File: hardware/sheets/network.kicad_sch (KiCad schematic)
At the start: 36 parts, among them J1 RJ45_LED, T1 13F-39MNL, U1 RTL8019AS, U2 AT93C46, U3 74LVC125A, U4 74LVC245A, U5 74HC138, Y1 20MHz

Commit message: addr_decode: hardwire LPT/IDE bases; centralize NIC + video disables (JP1-JP6)
LPT fixed at 0x378, IDE at 0x300 -- both base straps and their pull-ups
deleted ('138 ~Y1 now NC, the '00's ~A5 gate spare, IDE OR-leg takes raw
A5). The NIC and video disable jumpers move to addr_decode as JP5/JP6
with the same fit-to-disable sense as the rest: their gating hardware
stays local (the NIC's isolation '125 inside the 5V island, video's
firmware boot strap on GPIO42), only the jumper levels cross as
mxbus.PRIV_DIS -- video's documented firmware polarity inverts (high =
disabled; no firmware exists yet). Disable row is now a uniform JP1-JP6
(COM1/COM2/LPT/IDE/NIC/VID), bare board runs everything; network JP1/R6
and video JP1/R30 deleted, VID_BASE becomes video JP1. card_video's
wrapper re-adds a local DIS_VID strap (the documented PRIV lift
pattern). Docs/tables/decision logs aligned.

Co-Authored-By: Claude Fable 5 <noreply@anthropic.com>
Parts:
- removed JP1: NET_EN, Connector_PinHeader_2.54mm:PinHeader_1x02_P2.54mm_Vertical, symbol Connector_Generic:Conn_01x02
- removed R6: 10k, Resistor_SMD:R_0603_1608Metric, symbol Device:R
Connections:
- net ~{NET_EN} renamed DIS_NIC
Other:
- note added: "Disable = addr_decode JP5 (DIS_NIC high) -> '125 tri-states IRQ2 AND forces chip AEN high (all I/O ignored). Fully releases the bus for a sidecar card. Enabled by default (no jumper)."
- note removed: "JP1 closed = NIC enabled; open = R6 parks ~{NET_EN} high -> '125 tri-states IRQ2 AND forces chip AEN high (all I/O ignored). Fully releases the bus for a sidecar card."

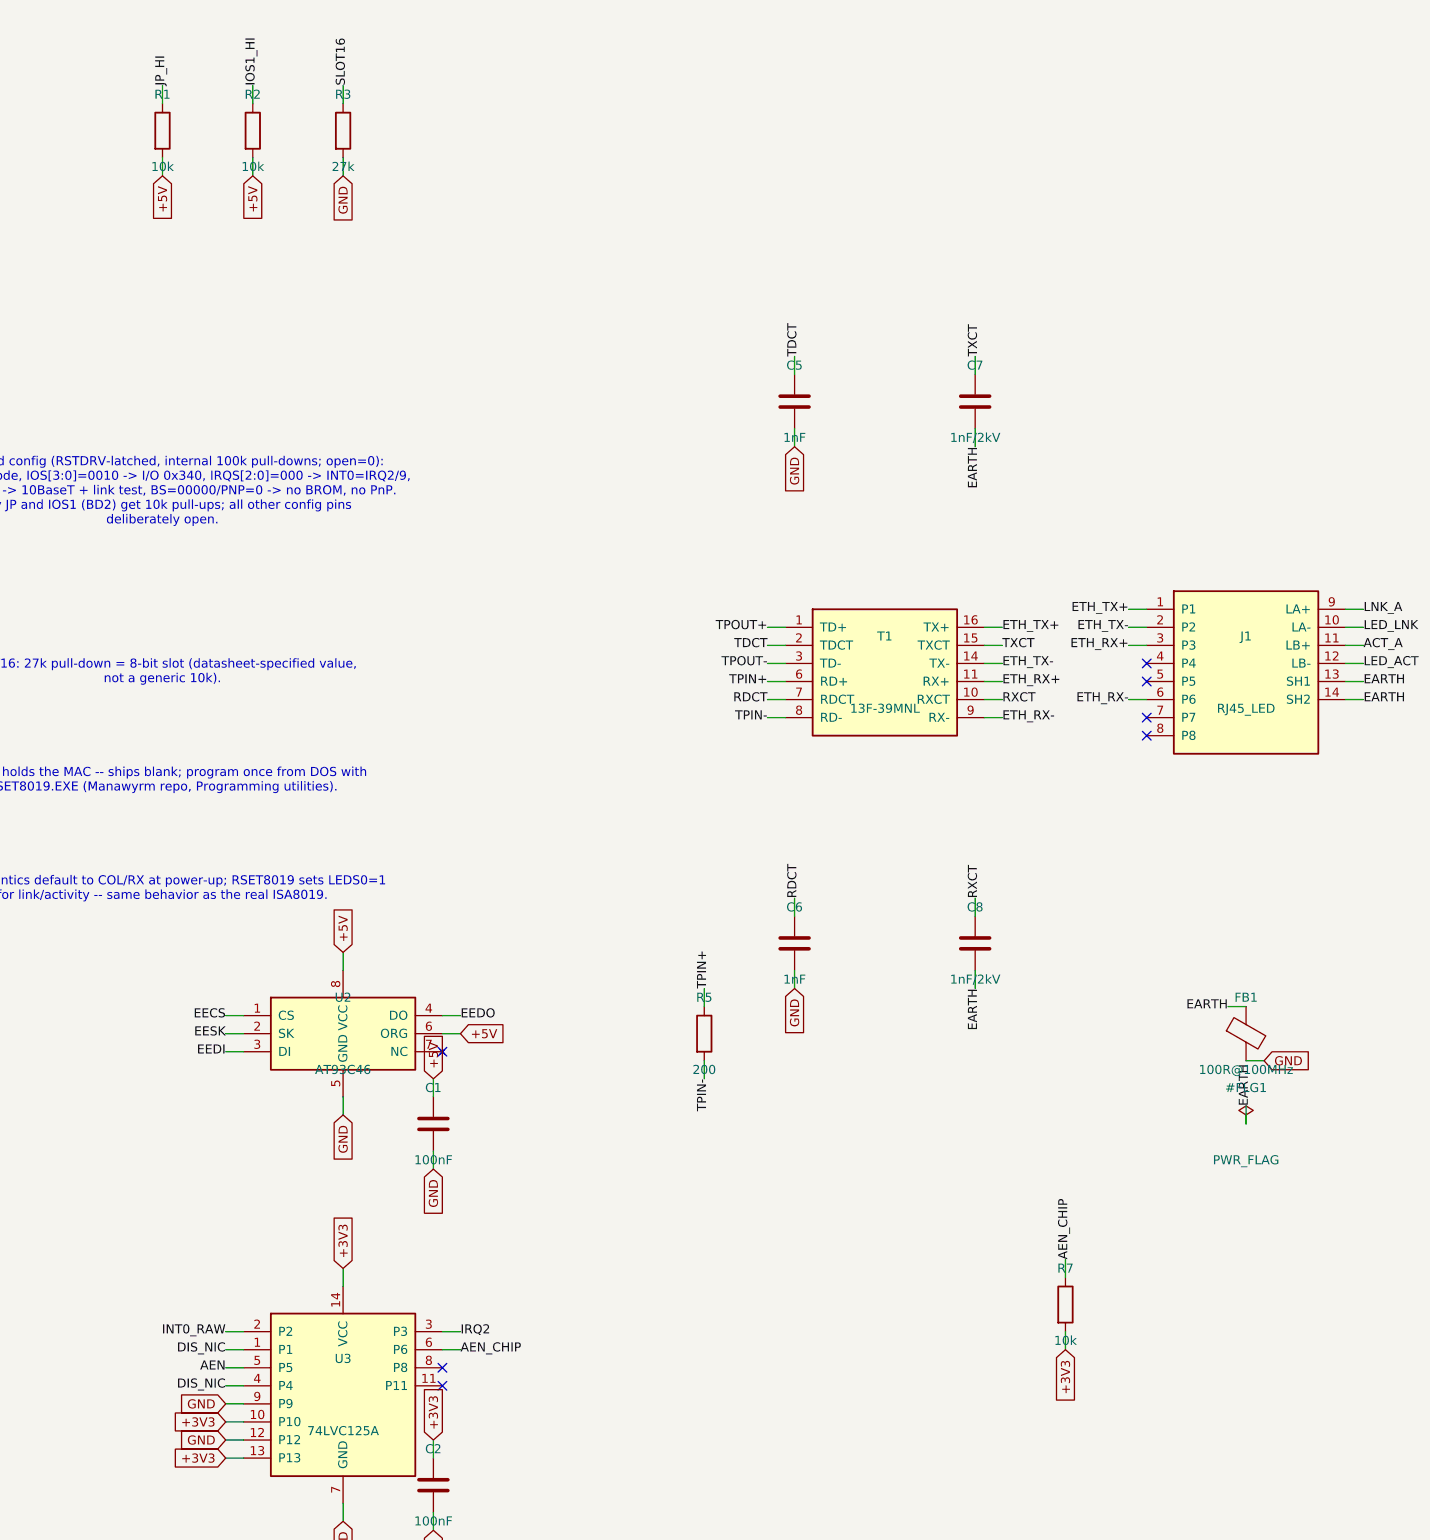
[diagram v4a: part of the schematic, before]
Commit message: Passives: basic-library audit + 4x resistor-array pull consolidation
Audit: every discrete R/C value was already JLC basic except the ferrite
beads -- swapped to basic Murata BLM18PG121SN1D (C14709, 120R@100MHz,
same family/role). The 100uF electrolytic and buck inductor stay
extended (zero fee-free parts exist in those subcategories). Pruned the
orphaned 5V-era 47nF/330nF MAX3241 cap entries.

Pull consolidation: 65 discrete 10k/4.7k rail pulls across 8 sheets
collapse into 18 basic 4-element isolated arrays (4D03WGJ0103T5E /
4D03WGJ0472T5E, element k = pins k/9-k; new mxbus.r_pack4 helper).
Isolated elements let packs mix rails; every net keeps its exact rail
and semantics (verified element-by-element in the netlist). RC/divider/
series/I2C resistors stay discrete. Board 452 -> 406 components; also
de-risks the sole basic 10k 0603 line (0 stock at audit). Audit
recorded in jlcpcb-sourcing.md.

Co-Authored-By: Claude Fable 5 <noreply@anthropic.com>
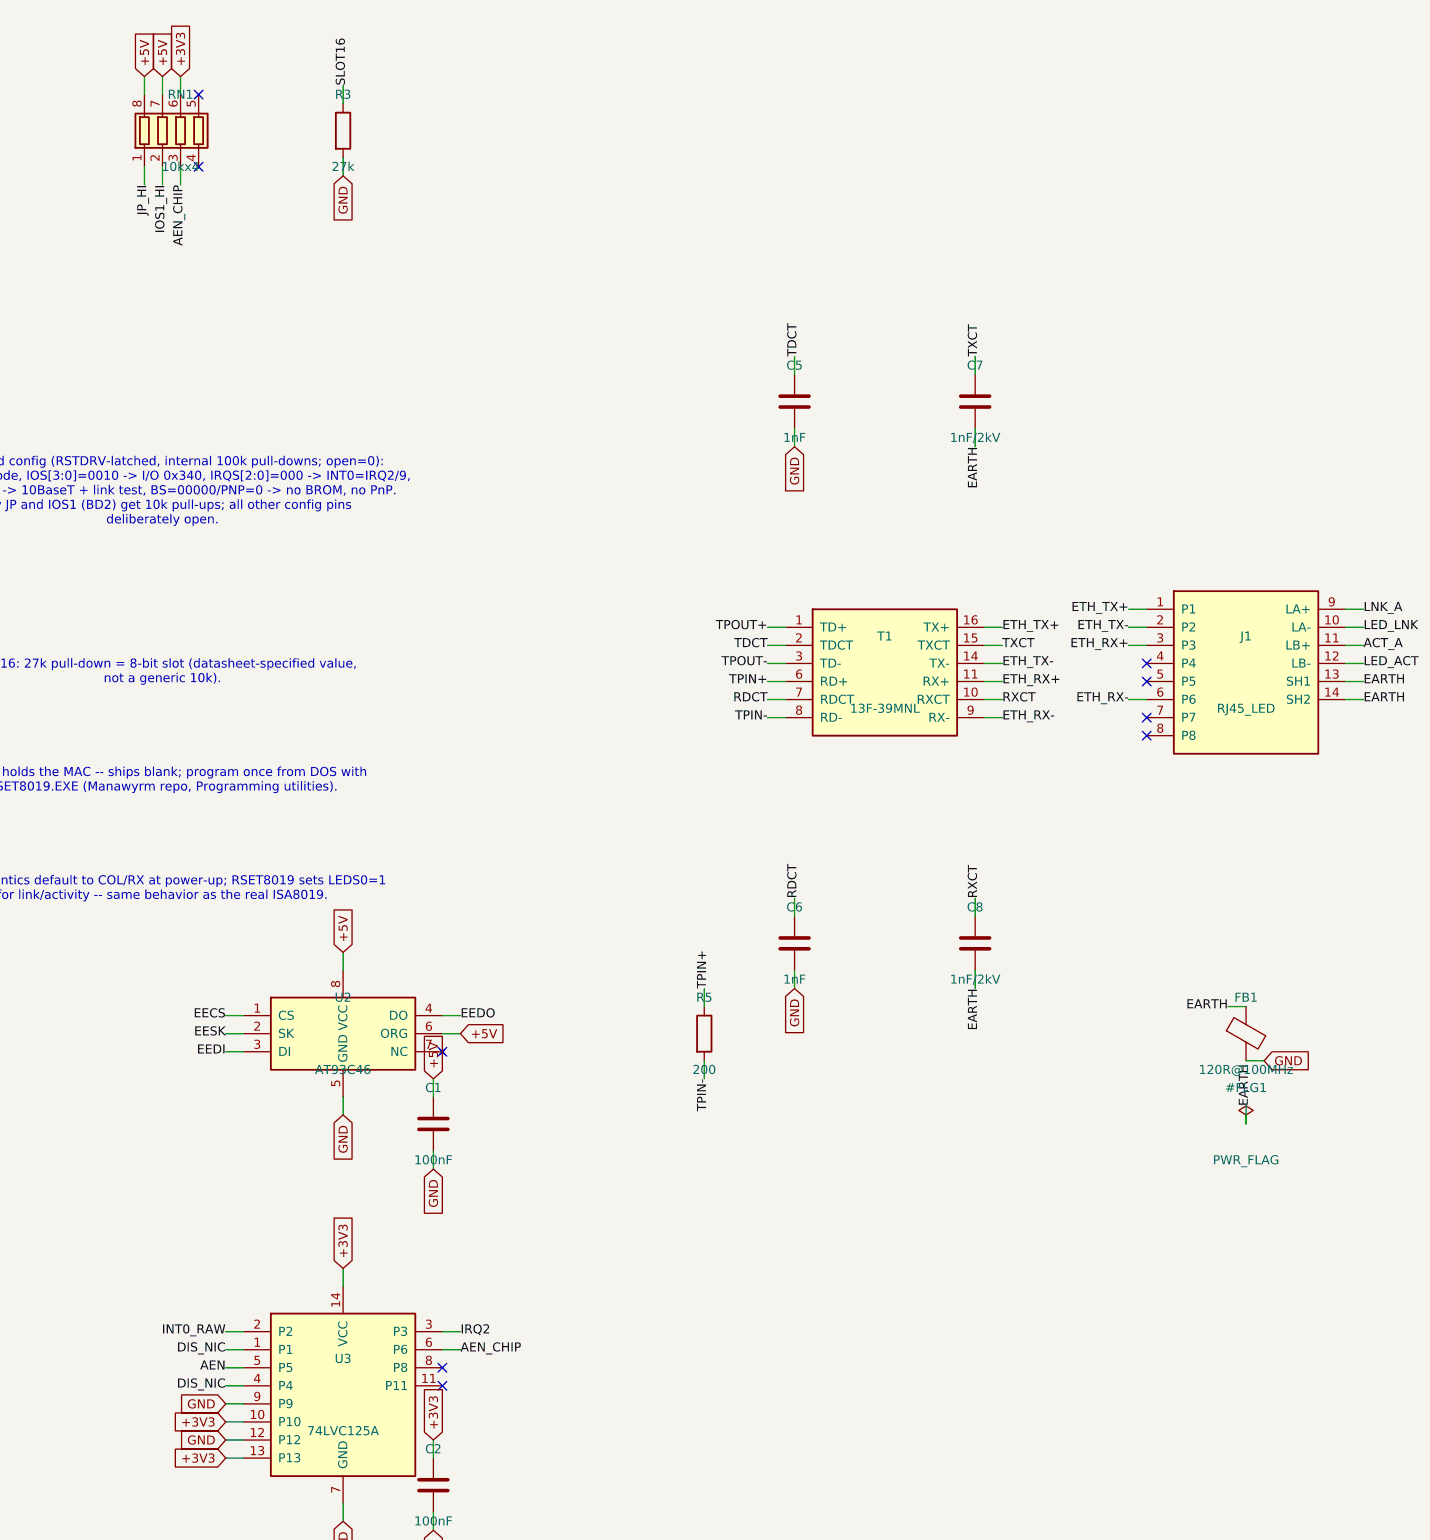
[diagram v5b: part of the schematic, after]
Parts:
- removed R2: 10k, Resistor_SMD:R_0603_1608Metric, symbol Device:R
- removed R3: 27k, Resistor_SMD:R_0603_1608Metric, symbol Device:R
- FB1: value 100R@100MHz -> 120R@100MHz; LCSC Part Num C160981 -> C14709
- R3: renamed from R4; value 1M -> 27k; LCSC Part Num C22935 -> C22967
- R4: renamed from R5; value 200 -> 1M; LCSC Part Num C8218 -> C22935
- R5: renamed from R7; value 10k -> 200; LCSC Part Num C25804 -> C8218
- RN1: renamed from R1; value 10k -> 10kx4; footprint Resistor_SMD:R_0603_1608Metric -> Resistor_SMD:R_Array_Convex_4x0603; symbol Device:R -> Device:R_Pack04; LCSC Part Num C25804 -> C29718
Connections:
- net +3V3: now also RN1.6 (R3.2); no longer R5.2
- net +5V: now also RN1.7 (R2.2), RN1.8 (R1.2); no longer RN1.2
- net AEN_CHIP: now also RN1.3 (R3.1); no longer R5.1
- net GND: now also R3.2
- net IOS1_HI: now also RN1.2 (R2.1)
- net SLOT16: now also R3.1
- net TPIN+: now also R5.1; no longer R4.1
- net TPIN-: now also R5.2; no longer R4.2
- net XTAL1: now also R4.1; no longer R3.1
- net XTAL2: now also R4.2; no longer R3.2
- no-connect marks 50 -> 52
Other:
- moved on the sheet: R3, R4, R5
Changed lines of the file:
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@@
 	(wire
 		(pts
-			(xy 228.6 21.59)
-			(xy 228.6 19.05)
+			(xy 226.06 30.48)
+			(xy 226.06 33.02)
 		)
 		(stroke
@@
 	)
 	(label "JP_HI"
-		(at 228.6 19.05 90)
+		(at 226.06 33.02 270)
 		(effects
 			(font
@@
 	(wire
 		(pts
-			(xy 228.6 29.21)
-			(xy 228.6 31.75)
+			(xy 226.06 20.32)
+			(xy 226.06 17.78)
 		)
 		(stroke
@@
 	(global_label "+5V"
 		(shape input)
-		(at 228.6 31.75 270)
+		(at 226.06 17.78 90)
 		(effects
 			(font
@@
 	(wire
 		(pts
-			(xy 241.3 21.59)
-			(xy 241.3 19.05)
+			(xy 228.6 30.48)
+			(xy 228.6 33.02)
 		)
 		(stroke
@@
 	)
 	(label "IOS1_HI"
-		(at 241.3 19.05 90)
+		(at 228.6 33.02 270)
 		(effects
 			(font
@@
 	(wire
 		(pts
-			(xy 241.3 29.21)
-			(xy 241.3 31.75)
+			(xy 228.6 20.32)
+			(xy 228.6 17.78)
 		)
 		(stroke
@@
 	(global_label "+5V"
 		(shape input)
-		(at 241.3 31.75 270)
+		(at 228.6 17.78 90)
 		(effects
 			(font
@@
 	(wire
 		(pts
-			(xy 254 21.59)
-			(xy 254 19.05)
+			(xy 231.14 30.48)
+			(xy 231.14 33.02)
 		)
 		(stroke
@@
 		)
 	)
-	(label "SLOT16"
-		(at 254 19.05 90)
+	(label "AEN_CHIP"
+		(at 231.14 33.02 270)
 		(effects
 			(font
@@
 	(wire
 		(pts
-			(xy 254 29.21)
-			(xy 254 31.75)
+			(xy 231.14 20.32)
+			(xy 231.14 17.78)
 		)
 		(stroke
@@
 		)
 	)
-	(global_label "GND"
+	(global_label "+3V3"
 		(shape input)
-		(at 254 31.75 270)
+		(at 231.14 17.78 90)
 		(effects
 			(font
@@
 		)
 	)
+	(no_connect
+		(at 233.68 30.48)
+	)
+	(no_connect
+		(at 233.68 20.32)
+	)
 	(wire
 		(pts
-			(xy 152.4 262.89)
-			(xy 152.4 260.35)
+			(xy 254 21.59)
+			(xy 254 19.05)
 		)
 		(stroke
@@
 		)
 	)
-	(label "XTAL1"
-		(at 152.4 260.35 90)
+	(label "SLOT16"
+		(at 254 19.05 90)
 		(effects
 			(font
@@
 	(wire
 		(pts
-			(xy 152.4 270.51)
-			(xy 152.4 273.05)
+			(xy 254 29.21)
+			(xy 254 31.75)
 		)
 		(stroke
@@
 		)
 	)
-	(label "XTAL2"
-		(at 152.4 273.05 270)
+	(global_label "GND"
+		(shape input)
+		(at 254 31.75 270)
 		(effects
 			(font
@@
 	(wire
 		(pts
-			(xy 304.8 148.59)
-			(xy 304.8 146.05)
+			(xy 152.4 262.89)
+			(xy 152.4 260.35)
 		)
 		(stroke
@@
 		)
 	)
-	(label "TPIN+"
-		(at 304.8 146.05 90)
+	(label "XTAL1"
+		(at 152.4 260.35 90)
 		(effects
 			(font
@@
 	(wire
 		(pts
-			(xy 304.8 156.21)
-			(xy 304.8 158.75)
+			(xy 152.4 270.51)
+			(xy 152.4 273.05)
 		)
 		(stroke
@@
 		)
 	)
-	(label "TPIN-"
-		(at 304.8 158.75 270)
+	(label "XTAL2"
+		(at 152.4 273.05 270)
 		(effects
 			(font
@@
 	(wire
 		(pts
-			(xy 355.6 186.69)
-			(xy 355.6 184.15)
+			(xy 304.8 148.59)
+			(xy 304.8 146.05)
 		)
 		(stroke
@@
 		)
 	)
-	(label "AEN_CHIP"
-		(at 355.6 184.15 90)
+	(label "TPIN+"
+		(at 304.8 146.05 90)
 		(effects
 			(font
@@
 	(wire
 		(pts
-			(xy 355.6 194.31)
-			(xy 355.6 196.85)
+			(xy 304.8 156.21)
+			(xy 304.8 158.75)
 		)
 		(stroke
@@
 		)
 	)
-	(global_label "+3V3"
-		(shape input)
-		(at 355.6 196.85 270)
+	(label "TPIN-"
+		(at 304.8 158.75 270)
 		(effects
 			(font
@@
 	)
 	(symbol
-		(lib_id "Device:R")
-		(at 228.6 25.4 0)
+		(lib_id "Device:R_Pack04")
+		(at 231.14 25.4 0)
 		(unit 1)
 		(exclude_from_sim no)
@@
 		(dnp no)
 		(fields_autoplaced yes)
-		(property "Reference" "R1"
-			(at 228.6 20.32 0)
+		(property "Reference" "RN1"
+			(at 231.14 20.32 0)
 			(effects
 				(font
@@
 			)
 		)
-		(property "Value" "10k"
-			(at 228.6 30.48 0)
+		(property "Value" "10kx4"
+			(at 231.14 30.48 0)
 			(effects
 				(font
@@
 			)
 		)
-		(property "Footprint" "Resistor_SMD:R_0603_1608Metric"
-			(at 228.6 25.4 0)
+		(property "Footprint" "Resistor_SMD:R_Array_Convex_4x0603"
+			(at 231.14 25.4 0)
 			(effects
 				(font
@@
 			)
 		)
-		(property "LCSC Part Num" "C25804"
-			(at 228.6 25.4 0)
+		(property "LCSC Part Num" "C29718"
+			(at 231.14 25.4 0)
 			(effects
 				(font
@@
 			)
 		)
-		(pin "1"
-		)
-		(pin "2"
+		(pin "8"
 		)
-		(instances
-			(project "mini-xt"
-				(path "/26736c46-8b40-5460-874f-03596d17270c/f3d0a5db-732a-509a-a7b0-e2622332c110"
-					(reference "R1201")
-					(unit 1)
-				)
-			)
+		(pin "1"
 		)
-	)
-	(symbol
-		(lib_id "Device:R")
-		(at 241.3 25.4 0)
-		(unit 1)
-		(exclude_from_sim no)
-		(in_bom yes)
-		(on_board yes)
-		(dnp no)
-		(fields_autoplaced yes)
-		(property "Reference" "R2"
-			(at 241.3 20.32 0)
-			(effects
-				(font
-					(size 1.27 1.27)
-				)
-			)
+		(pin "7"
 		)
-		(property "Value" "10k"
-			(at 241.3 30.48 0)
-			(effects
-				(font
-					(size 1.27 1.27)
-				)
-			)
+		(pin "2"
 		)
-		(property "Footprint" "Resistor_SMD:R_0603_1608Metric"
-			(at 241.3 25.4 0)
-			(effects
-				(font
-					(size 1.27 1.27)
-				)
-				(hide yes)
-			)
+		(pin "6"
 		)
-		(property "LCSC Part Num" "C25804"
-			(at 241.3 25.4 0)
-			(effects
-				(font
-					(size 1.27 1.27)
-				)
-				(hide yes)
-			)
+		(pin "3"
 		)
-		(pin "1"
+		(pin "5"
 		)
-		(pin "2"
+		(pin "4"
 		)
 		(instances
 			(project "mini-xt"
 				(path "/26736c46-8b40-5460-874f-03596d17270c/f3d0a5db-732a-509a-a7b0-e2622332c110"
-					(reference "R1202")
+					(reference "RN1201")
 					(unit 1)
 				)
@@
 	(symbol
 		(lib_id "Device:R")
-		(at 355.6 190.5 0)
-		(unit 1)
-		(exclude_from_sim no)
-		(in_bom yes)
-		(on_board yes)
-		(dnp no)
-		(fields_autoplaced yes)
-		(property "Reference" "R7"
-			(at 355.6 185.42 0)
-			(effects
-				(font
-					(size 1.27 1.27)
-				)
-			)
-		)
-		(property "Value" "10k"
-			(at 355.6 195.58 0)
-			(effects
-				(font
-					(size 1.27 1.27)
-				)
-			)
-		)
-		(property "Footprint" "Resistor_SMD:R_0603_1608Metric"
-			(at 355.6 190.5 0)
-			(effects
-				(font
-					(size 1.27 1.27)
-				)
-				(hide yes)
-			)
-		)
-		(property "LCSC Part Num" "C25804"
-			(at 355.6 190.5 0)
-			(effects
-				(font
-					(size 1.27 1.27)
-				)
-				(hide yes)
-			)
-		)
-		(pin "1"
-		)
-		(pin "2"
-		)
-		(instances
-			(project "mini-xt"
-				(path "/26736c46-8b40-5460-874f-03596d17270c/f3d0a5db-732a-509a-a7b0-e2622332c110"
-					(reference "R1207")
-					(unit 1)
-				)
-			)
-		)
-	)
-	(symbol
-		(lib_id "Device:R")
 		(at 368.3 254 0)
 		(unit 1)
@@
 			)
 		)
-		(property "Value" "100R@100MHz"
+		(property "Value" "120R@100MHz"
 			(at 381 157.48 0)
 			(effects
@@
 			)
 		)
-		(property "LCSC Part Num" "C160981"
+		(property "LCSC Part Num" "C14709"
 			(at 381 152.4 0)
 			(effects
